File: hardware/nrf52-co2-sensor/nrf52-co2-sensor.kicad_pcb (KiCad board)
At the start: 4 copper layers, 28 parts, among them J1 USB4105-GF-A, J2 SCD30, J3 Conn_01x02, J4 SWD, SW1 SW_Push, U1 USBLC6-2P6, U2 TLV75533PDBV, U3 MDBT50Q-1MV2

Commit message: Last commit before power rework
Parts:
- moved R8 3.58 mm to (112.0, 89.0), turned to -90 degrees
- moved SW1 3.23 mm to (106.4, 89.5), turned to -90 degrees
- moved D1 2.55 mm to (110.5, 89.5), turned to -90 degrees
- moved J4 1.80 mm to (113.5, 90.5)
- moved J2 0.50 mm to (99.0, 88.5)
- moved R7 0.46 mm to (113.5, 88.5)
- moved U3 0.25 mm to (118.2, 81.8)

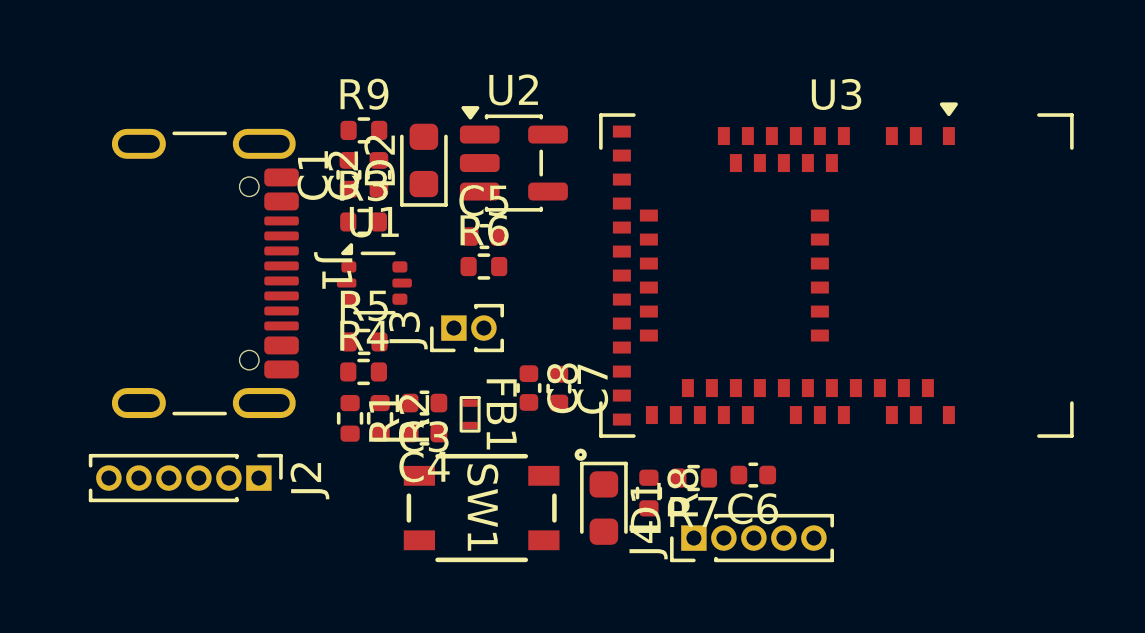
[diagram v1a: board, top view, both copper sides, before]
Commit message: first iteration of pcb layout ready for review
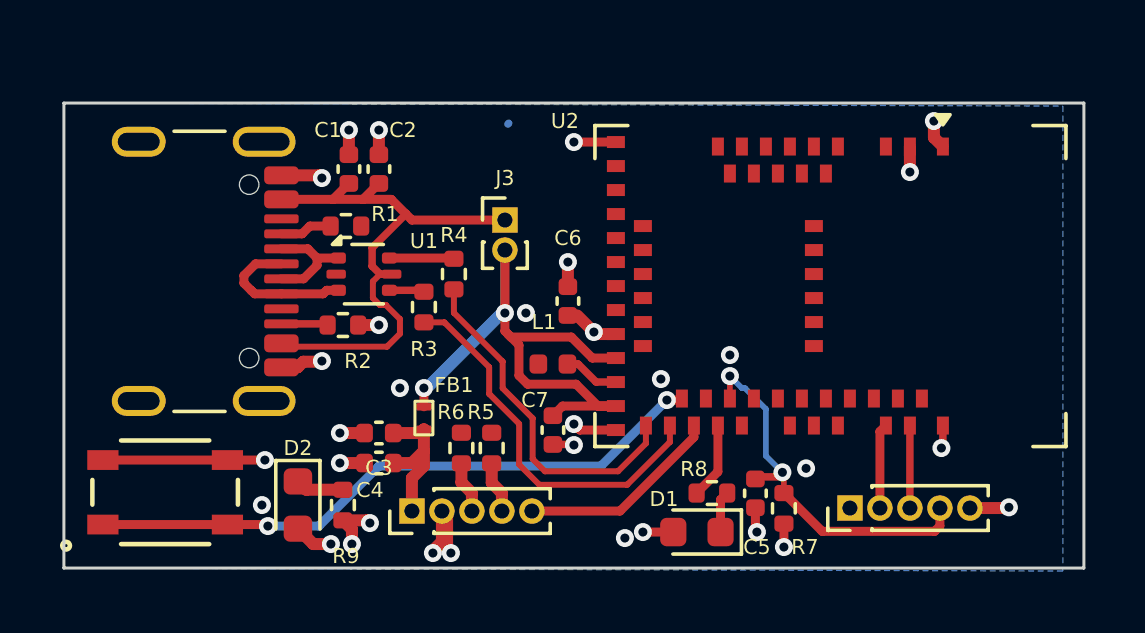
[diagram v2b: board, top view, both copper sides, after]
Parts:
- removed C8: 10uf, Capacitor_SMD:C_0402_1005Metric
- removed U3: MDBT50Q-1MV2, RF_Module:Raytac_MDBT50Q
- added L1: 10uH, Inductor_SMD:L_0402_1005Metric, F.Cu at (108.8, 84.7)
- C5: value 2.2uf -> 100nF
- C6: value 100nF -> 10uf
- C7: value 0.1uF -> 10uf
- J2: footprint Connector_PinHeader_1.00mm:PinHeader_1x06_P1.00mm_Vertical -> Connector_PinHeader_1.00mm:PinHeader_1x05_P1.00mm_Vertical
- R1, R2: value 4.7k -> 5.1k
- R3, R4: value 5.1k -> 22
- R5, R6: value 22 -> 4.7k
- U2: value TLV75533PDBV -> MDBT50Q-1MV2; footprint Package_TO_SOT_SMD:SOT-23-5 -> RF_Module:Raytac_MDBT50Q
- moved R9 12.5 mm to (101.8, 89.4), turned to -90 degrees
- moved C5 12.4 mm to (115.5, 89.0), turned to 90 degrees
- moved D2 12.2 mm to (100.3, 89.4), turned to -90 degrees
- moved U2 11.3 mm to (118.0, 82.1), turned to -90 degrees
- moved SW1 10.6 mm to (95.9, 89.0), turned to 90 degrees
- moved C6 8.48 mm to (109.3, 82.6), turned to -90 degrees
- moved R1 6.41 mm to (101.9, 80.1), turned to 0 degrees
- moved R6 6.10 mm to (105.8, 87.5), turned to 90 degrees
- moved R5 5.53 mm to (106.8, 87.5), turned to 90 degrees
- moved J4 5.30 mm to (118.7, 89.5)
- moved J2 5.22 mm to (104.1, 89.6), turned to 90 degrees
- moved R4 4.44 mm to (105.5, 81.7), turned to -90 degrees
- moved J3 3.98 mm to (107.2, 79.9), turned to 0 degrees
- moved R3 3.48 mm to (104.5, 82.8), turned to 90 degrees
- moved R2 3.35 mm to (101.8, 83.4), turned to 0 degrees
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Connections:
- C1 pad 1: /VBUS -> /VBUS_USB
- C2 pad 1: /VBUS -> /VBUS_USB
- C3 pad 1: /3V3_SENS -> /VBUS_SENS
- C4 pad 1: /3V3_SENS -> /VBUS_SENS
- C5 pad 2: /LDO_IN -> /RESETN
- C6 pad 2: /RESETN -> /3V_VDD
- C7 pad 1: +3.3V -> GND
- C7 pad 2: GND -> /VBUS
- D1 pad 2: +3.3V -> /3V_VDD
- D2 pad 2: +3.3V -> /3V_VDD
- J1 pad A4: /VBUS -> /VBUS_USB
- J1 pad A9: /VBUS -> /VBUS_USB
- J1 pad B4: /VBUS -> /VBUS_USB
- J1 pad B9: /VBUS -> /VBUS_USB
- J2 pad 1: /3V3_SENS -> /VBUS_SENS
- J2 pad 3: /SDA -> /SCL
- J2 pad 4: /SCL -> /SDA
- J2 pad 5: /GPIO P0.14 -> /GPIO P0.13
- J3 pad 1: /VBUS -> /VBUS_USB
- J3 pad 2: /LDO_IN -> /VBUS
- J4 pad 1: +3.3V -> /3V_VDD
- R1 pad 1: /SCL -> Net-(J1-CC1)
- R1 pad 2: /3V3_SENS -> GND
- R2 pad 1: /SDA -> Net-(J1-CC2)
- R2 pad 2: /3V3_SENS -> GND
- R3 pad 1: Net-(J1-CC1) -> /D+_MCU
- R3 pad 2: GND -> Net-(R3-Pad2)
- R4 pad 1: Net-(J1-CC2) -> Net-(R4-Pad1)
- R4 pad 2: GND -> /D-_MCU
- R5 pad 1: /usb_D+ -> /SDA
- R5 pad 2: Net-(R5-Pad2) -> /3V_VDD
- R6 pad 1: Net-(R6-Pad1) -> /SCL
- R6 pad 2: /usb_D- -> /3V_VDD
- R7 pad 2: +3.3V -> /3V_VDD
- R8 pad 2: /GPIO P0.13 -> /GPIO P0.15
- SW1 pad 1: /GPIO P0.15 -> /GPIO P0.14
- SW1 pad 2: /GPIO P0.15 -> /GPIO P0.14
- U1 pad 4: Net-(R5-Pad2) -> Net-(R3-Pad2)
- U1 pad 5: /VBUS -> /VBUS_USB
- U1 pad 6: Net-(R6-Pad1) -> Net-(R4-Pad1)
- U2 pad 1: /LDO_IN -> GND
- U2 pad 3: /LDO_IN -> unconnected-(U2B-P1.10-Pad3)
- U2 pad 5: +3.3V -> unconnected-(U2B-P1.12-Pad5)
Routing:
- net GND: track 0.00 -> 26.1 mm, vias 0 -> 28
- net /GPIO P0.14: track 0.00 -> 21.1 mm, vias 0 -> 2
- net /VBUS: track 0.00 -> 20.6 mm, vias 0 -> 2
- net /VBUS_USB: track 0.00 -> 19.0 mm
- net /D+_MCU: track 0.00 -> 12.9 mm
- net /RESETN: track 0.00 -> 12.6 mm, vias 0 -> 2
- net /D-_MCU: track 0.00 -> 11.7 mm
- net /GPIO P0.13: track 0.00 -> 6.84 mm
- net /VBUS_SENS: track 0.00 -> 5.15 mm
- net /D+: track 0.00 -> 5.01 mm
- net /3V_VDD: track 0.00 -> 4.96 mm, vias 0 -> 4
- net /D-: track 0.00 -> 3.65 mm
- net /SWDIO: track 0.00 -> 2.83 mm
- net /SWCLK: track 0.00 -> 2.75 mm
- net /GPIO P0.15: track 0.00 -> 2.54 mm
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- added copper zone on B.Cu, net /3V_VDD
- added copper zone on In1.Cu, net GND
- added copper zone on In2.Cu, net GND
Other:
- board outline added: 34 x 15.5 mm

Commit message: Finished PCB Layout and BOM read for review
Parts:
- removed C1: 0.1uf, Capacitor_SMD:C_0402_1005Metric
- removed C2: 10uf, Capacitor_SMD:C_0402_1005Metric
- removed FB1: 600 @ 100Mhz, nrf52-co2-sensor:BLM15AX601SN1D
- added C10: 10nf, Capacitor_SMD:C_0402_1005Metric, F.Cu at (140.5, 160.8)
- added C8: 47uf, Capacitor_SMD:C_0805_2012Metric, F.Cu at (110.8, 164.3)
- added C9: 0.1uf, Capacitor_SMD:C_0402_1005Metric, F.Cu at (130.6, 155.6)
- added D3: 1N914, Diode_SMD:Nexperia_CFP3_SOD-123W, F.Cu at (111.9, 168.8)
- added J6: Conn_01x02, Connector_JST:JST_XH_B2B-XH-AM_1x02_P2.50mm_Vertical, F.Cu at (98.5, 170.2)
- added J7: Conn_01x02, Connector_PinHeader_2.54mm:PinHeader_1x02_P2.54mm_Vertical, F.Cu at (114.2, 159.3)
- added Q2: Q_NPN_BEC, Package_TO_SOT_SMD:SOT-23, F.Cu at (113.7, 163.2)
- added R10: 150, Resistor_SMD:R_0402_1005Metric, F.Cu at (113.2, 165.8)
- added R11: 2.2M, Resistor_SMD:R_0402_1005Metric, F.Cu at (140.5, 163.3)
- added R12: 1M, Resistor_SMD:R_0402_1005Metric, F.Cu at (140.7, 167.1)
- C6, C7: footprint Capacitor_SMD:C_0402_1005Metric -> Capacitor_SMD:C_0805_2012Metric
- J2, J4: footprint Connector_PinHeader_1.00mm:PinHeader_1x05_P1.00mm_Vertical -> Connector_PinHeader_2.54mm:PinHeader_1x05_P2.54mm_Vertical
- J3: value Conn_01x02 -> Conn_01x03; footprint Connector_PinHeader_1.00mm:PinHeader_1x02_P1.00mm_Vertical -> Connector_PinHeader_2.54mm:PinHeader_1x03_P2.54mm_Vertical
- R8: value 4.7k -> 2.2k
- moved U2 84.5 mm to (133.7, 165.2), turned to 180 degrees
- moved J3 80.5 mm to (97.2, 159.8), turned to 90 degrees
- moved R8 77.2 mm to (147.4, 158.6), turned to -90 degrees
- moved R6 77.0 mm to (141.9, 155.5), turned to -90 degrees
- moved R4 77.0 mm to (127.3, 155.5)
- moved D1 76.8 mm to (149.0, 158.5), turned to -90 degrees
- moved C6 76.6 mm to (133.8, 155.2)
- moved J2 76.1 mm to (147.0, 152.5), turned to -90 degrees
- moved C3 76.1 mm to (146.4, 149.5), turned to 90 degrees
- moved C4 75.8 mm to (147.4, 149.5), turned to 90 degrees
- moved R3 75.7 mm to (126.1, 155.4)
- moved R9 75.6 mm to (105.0, 164.9)
- moved R5 75.2 mm to (139.3, 155.3), turned to -90 degrees
- moved D2 75.2 mm to (103.5, 164.5)
- moved C5 74.6 mm to (127.4, 162.7)
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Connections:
- net /D+_MCU renamed /D_MCU+
- net /D-_MCU renamed /D_MCU-
- net /GPIO P0.13 renamed /SCD30_RDY
- net /GPIO P0.14 renamed /BUTTON_1
- net /GPIO P0.15 renamed /LED_1
- net /VBUS_SENS renamed /POWER_SENS
- net Net-(J1-CC1) renamed /CC1
- net Net-(J1-CC2) renamed /CC2
- net Net-(R3-Pad2) renamed /D1+
- net Net-(R4-Pad1) renamed /D1-
- J1 pad A4: /VBUS_USB -> /VBUS
- J1 pad A9: /VBUS_USB -> /VBUS
- J1 pad B4: /VBUS_USB -> /VBUS
- J1 pad B9: /VBUS_USB -> /VBUS
- J2 pad 3: /SCL -> /SCD30_SCL
- J2 pad 4: /SDA -> /SCD30_SDA
- J3 pad 1: /VBUS_USB -> /VBUS
- J3 pad 2: /VBUS -> /POWER_RAW
- R5 pad 1: /SDA -> /SCD30_SDA
- R6 pad 1: /SCL -> /SCD30_SCL
- U1 pad 5: /VBUS_USB -> /VBUS
- U2 pad 16: unconnected-(U2B-P0.27-Pad16) -> /SCD30_SCL
- U2 pad 19: unconnected-(U2B-P0.26-Pad19) -> /SCD30_SDA
- U2 pad 30: /VBUS -> /POWER_RAW
- U2 pad 9: unconnected-(U2B-P0.03/AINI-Pad9) -> /POWER_ADC
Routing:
- net /POWER_SENS: track 5.15 -> 67.1 mm, vias 0 -> 2
- net /POWER_RAW: track 0.00 -> 43.6 mm, vias 0 -> 1
- net /VBUS: track 20.6 -> 54.7 mm
- net /SCD30_SDA: track 0.00 -> 20.2 mm
- net /LED_1: track 2.54 -> 22.6 mm, vias 0 -> 2
- net /VBUS_USB: track 19.0 -> 0.00 mm
- net /D1-: track 2.16 -> 20.7 mm
- net /D1+: track 1.17 -> 19.4 mm
- net /POWER_ADC: track 0.00 -> 13.4 mm
- net /External Power: track 0.00 -> 12.0 mm
- net /3V_VDD: track 4.96 -> 14.8 mm, vias 4 -> 6
- net /SCD30_SCL: track 0.00 -> 8.32 mm
- net /SCD30_RDY: track 6.84 -> 14.6 mm, vias 0 -> 2
- net /RESETN: track 12.6 -> 20.0 mm
- net /BASE: track 0.00 -> 7.33 mm
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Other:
- board size 34 x 15.5 mm -> 54.6 x 27 mm
- rule pad_to_mask_clearance: 0 -> 0.0381
- board text added: "3V"
- board text added: "BATTERY_IN"
- board text added: "BJT BYPASS"
- board text added: "GND"
- board text added: "POWER SELECT USB:1-2 EXT5V:2-3"
- board text added: "RESET"
- board text added: "SWCLK"
- board text added: "SWDIO"
